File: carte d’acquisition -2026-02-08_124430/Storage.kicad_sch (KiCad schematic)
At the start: 15 parts, among them J5 Micro_SD_Card_Det1

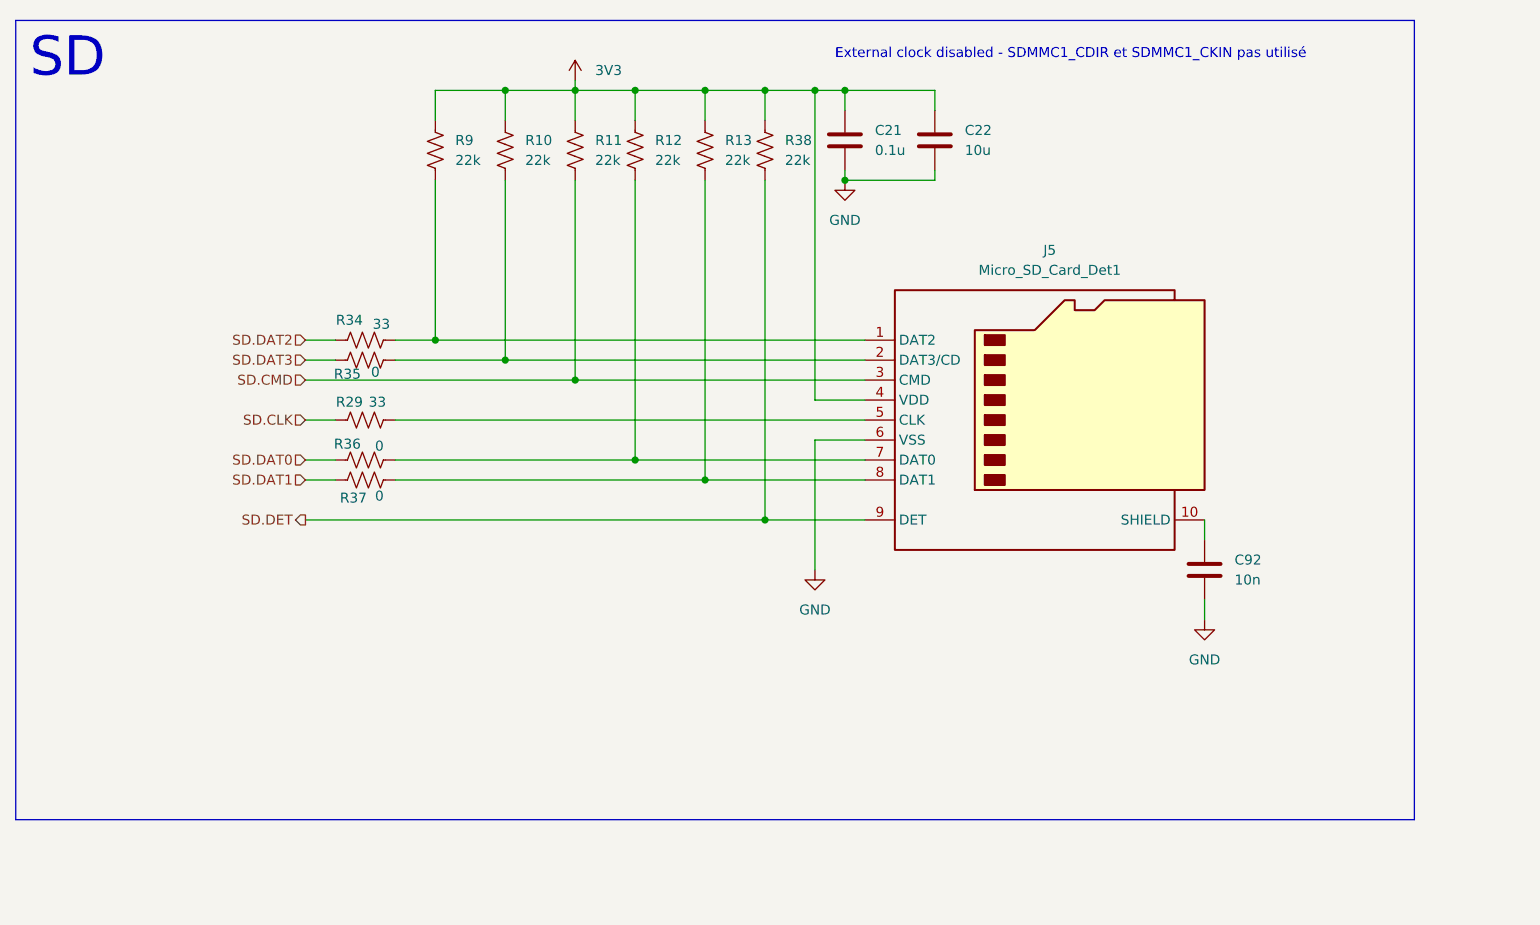
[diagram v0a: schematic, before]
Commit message: Power et maj can et sd
Modifications sur l'alim selon le schéma sur Canvas et mise à jour du can et carte sd
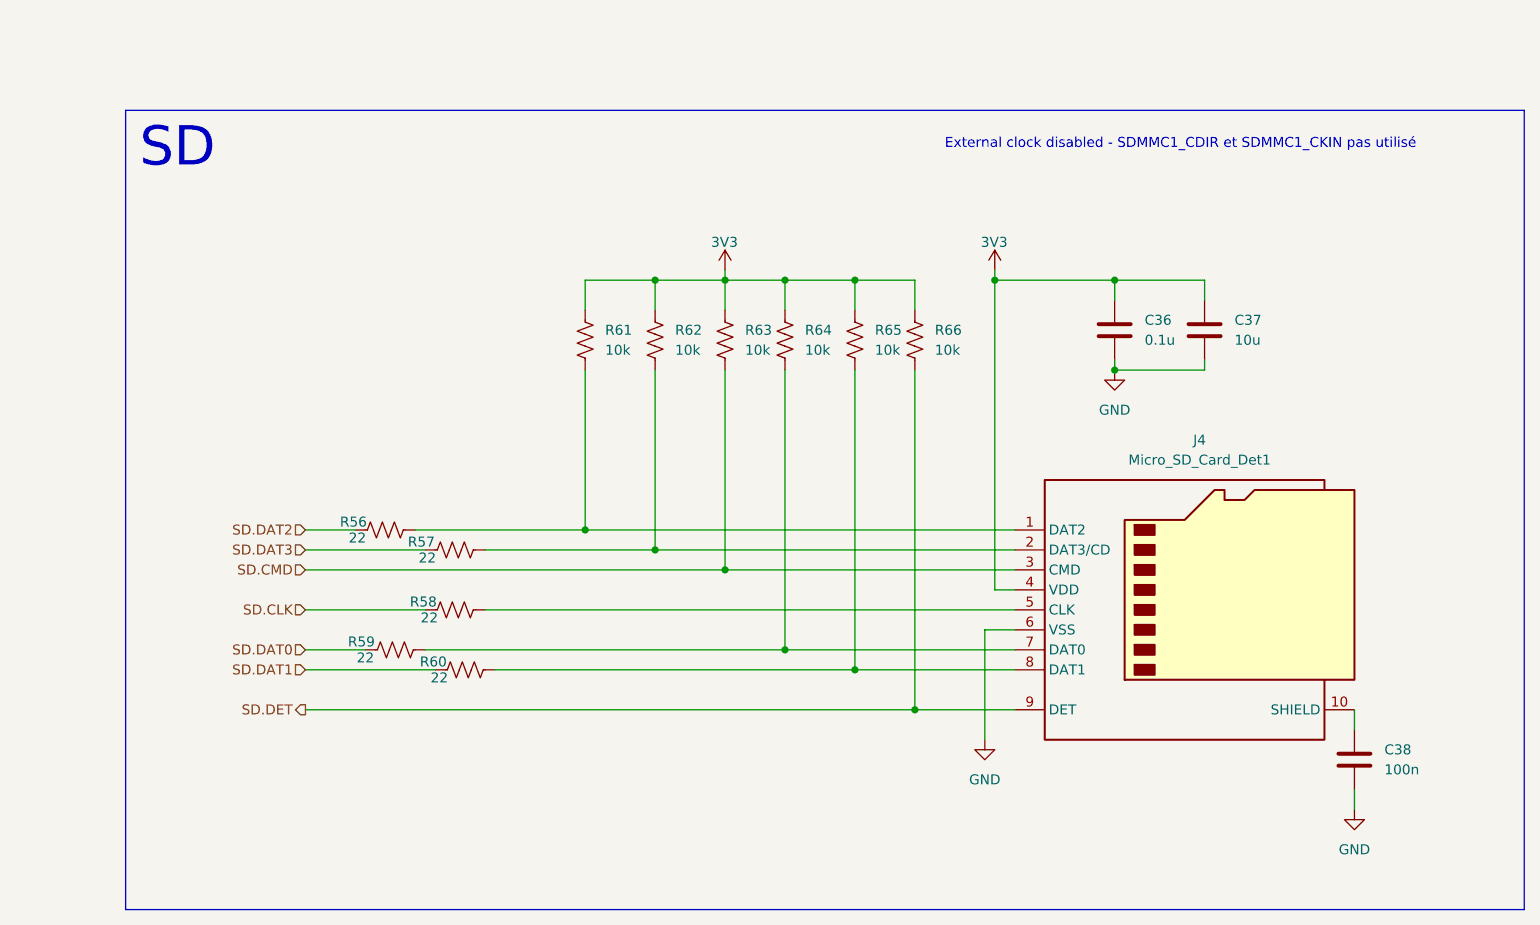
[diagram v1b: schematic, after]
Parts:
- removed C21: 0.1u, symbol Device:C
- removed C22: 10u, symbol Device:C
- removed C92: 10n, symbol Device:C
- removed J5: Micro_SD_Card_Det1, symbol Connector:Micro_SD_Card_Det1
- removed R10, R11, R12, R13, R38, R9: 22k, symbol Device:R_US
- removed R29, R34: 33, symbol Device:R_US
- removed R35, R36, R37: 0, symbol Device:R_US
- added C36: 0.1u, Capacitor_SMD:C_0603_1608Metric, symbol Device:C
- added C37: 10u, Capacitor_SMD:C_0603_1608Metric, symbol Device:C
- added C38: 100n, symbol Device:C
- added J4: Micro_SD_Card_Det1, symbol Connector:Micro_SD_Card_Det1
- added R56, R57, R58, R59, R60: 22, symbol Device:R_US
- added R61, R62, R63, R64, R65, R66: 10k, symbol Device:R_US
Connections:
- net 3V3: now also C36.1, C37.1, J4.4 (VDD), R61.1, R62.1, R63.1, R64.1, R65.1, R66.1
- net GND: now also C36.2, C37.2, C38.2, J4.6 (VSS)
- net SD.CLK: now also R58.1
- net SD.CMD: now also J4.3 (CMD), R63.2
- net SD.DAT0: now also R59.1
- net SD.DAT1: now also R60.1
- net SD.DAT2: now also R56.1
- net SD.DAT3: now also R57.1
- net SD.DET: now also J4.9 (DET), R66.2
- new net: J4.5 (CLK), R58.2
- new net: J4.1 (DAT2), R56.2, R61.2
- new net: C38.1, J4.10 (SHIELD)
- new net: J4.2 (DAT3/CD), R57.2, R62.2
- new net: J4.7 (DAT0), R59.2, R64.2
- new net: J4.8 (DAT1), R60.2, R65.2

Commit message: Mis a jour plusieurs circuit et ajouter beaucoup de footprint manquant
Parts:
- C38: footprint (none) -> Capacitor_SMD:C_0603_1608Metric
- J4: footprint (none) -> UserFootprints:GCT_MEM2075-00-140-01-A
- R56, R57, R58, R59, R60, R61, R62, R63, R64, R65, R66: footprint (none) -> Resistor_SMD:R_0603_1608Metric
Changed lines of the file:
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@@
 			)
 		)
-		(property "Footprint" ""
+		(property "Footprint" "Resistor_SMD:R_0603_1608Metric"
 			(at 104.394 113.284 90)
 			(effects
@@
 			)
 		)
-		(property "Footprint" ""
+		(property "Footprint" "UserFootprints:GCT_MEM2075-00-140-01-A"
 			(at 250.19 96.52 0)
 			(effects
@@
 			)
 		)
-		(property "Footprint" ""
+		(property "Footprint" "Resistor_SMD:R_0603_1608Metric"
 			(at 163.576 80.264 90)
 			(effects
@@
 			)
 		)
-		(property "Footprint" ""
+		(property "Footprint" "Capacitor_SMD:C_0603_1608Metric"
 			(at 219.4052 137.16 0)
 			(effects
@@
 			)
 		)
-		(property "Footprint" ""
+		(property "Footprint" "Resistor_SMD:R_0603_1608Metric"
 			(at 147.066 80.264 90)
 			(effects
@@
 			)
 		)
-		(property "Footprint" ""
+		(property "Footprint" "Resistor_SMD:R_0603_1608Metric"
 			(at 105.664 120.904 90)
 			(effects
@@
 			)
 		)
-		(property "Footprint" ""
+		(property "Footprint" "Resistor_SMD:R_0603_1608Metric"
 			(at 104.394 105.664 90)
 			(effects
@@
 			)
 		)
-		(property "Footprint" ""
+		(property "Footprint" "Resistor_SMD:R_0603_1608Metric"
 			(at 139.446 80.264 90)
 			(effects
@@
 			)
 		)
-		(property "Footprint" ""
+		(property "Footprint" "Resistor_SMD:R_0603_1608Metric"
 			(at 130.556 80.264 90)
 			(effects
@@
 			)
 		)
-		(property "Footprint" ""
+		(property "Footprint" "Resistor_SMD:R_0603_1608Metric"
 			(at 96.774 118.364 90)
 			(effects
@@
 			)
 		)
-		(property "Footprint" ""
+		(property "Footprint" "Resistor_SMD:R_0603_1608Metric"
 			(at 95.504 103.124 90)
 			(effects
@@
 			)
 		)
-		(property "Footprint" ""
+		(property "Footprint" "Resistor_SMD:R_0603_1608Metric"
 			(at 155.956 80.264 90)
 			(effects
@@
 			)
 		)
-		(property "Footprint" ""
+		(property "Footprint" "Resistor_SMD:R_0603_1608Metric"
 			(at 121.666 80.264 90)
 			(effects
